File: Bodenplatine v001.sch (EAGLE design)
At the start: 113 parts, among them K1 RY612012, K2 RY612012, K3 RY612012, K4 RY612012, K5 RY612012, K6 RY612012, K7 RY612012, K8 RY612012, K9 RY612012, Q1 BC846BLT1SMD, Q2 BC846BLT1SMD, Q3 BC846BLT1SMD, Q4 BC846BLT1SMD, Q5 BC846BLT1SMD, Q6 BC846BLT1SMD, Q7 BC846BLT1SMD, Q8 BC846BLT1SMD, Q9 BC846BLT1SMD, X1 SPRINGCON_AST125_5X2, X10 SPRINGCON_AST125_3X2, X11 SPRINGCON_AST125_4X2, X12 SPRINGCON_AST125_4X2, X13 SPRINGCON_AST125_5X2, X14 236-403, X15 236-402, X2 SPRINGCON_AST125_5X2, X3 SPRINGCON_AST125_5X2, X4 SPRINGCON_AST125_5X2, X5 SPRINGCON_AST125_5X2, X6 SPRINGCON_AST125_5X2, X7 SPRINGCON_AST125_5X2, X8 SPRINGCON_AST125_5X2, X9 SPRINGCON_AST125_5X2

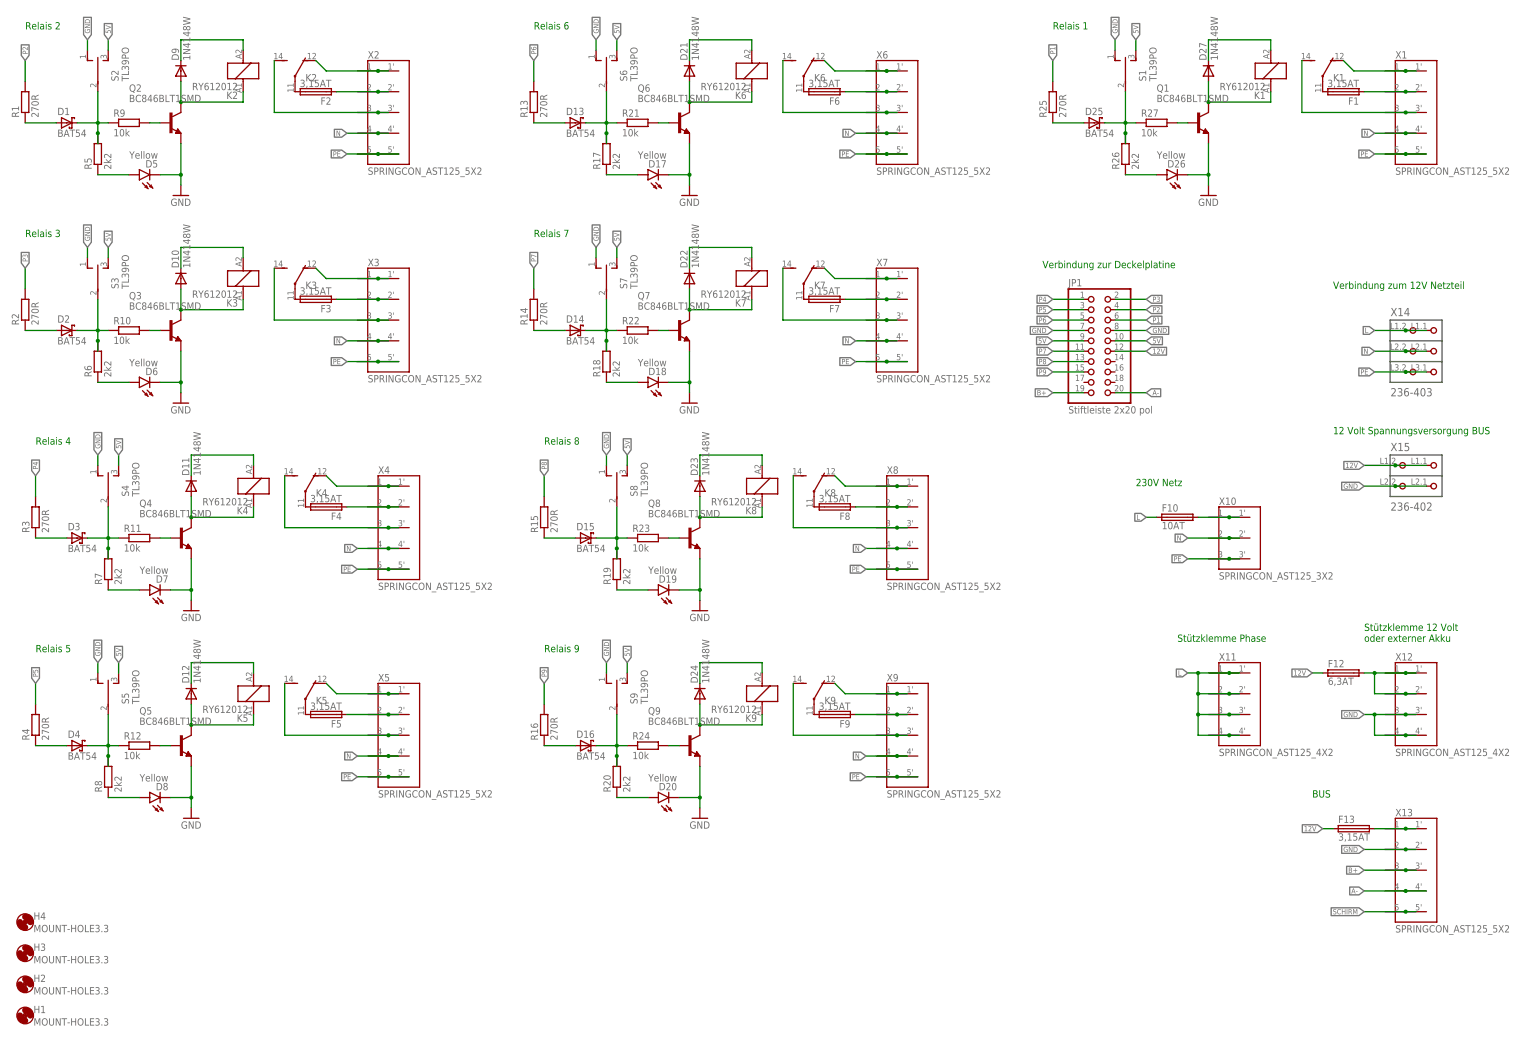
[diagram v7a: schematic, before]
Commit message: Alle Connectoren mit 2 Pins richtig verbunden.@
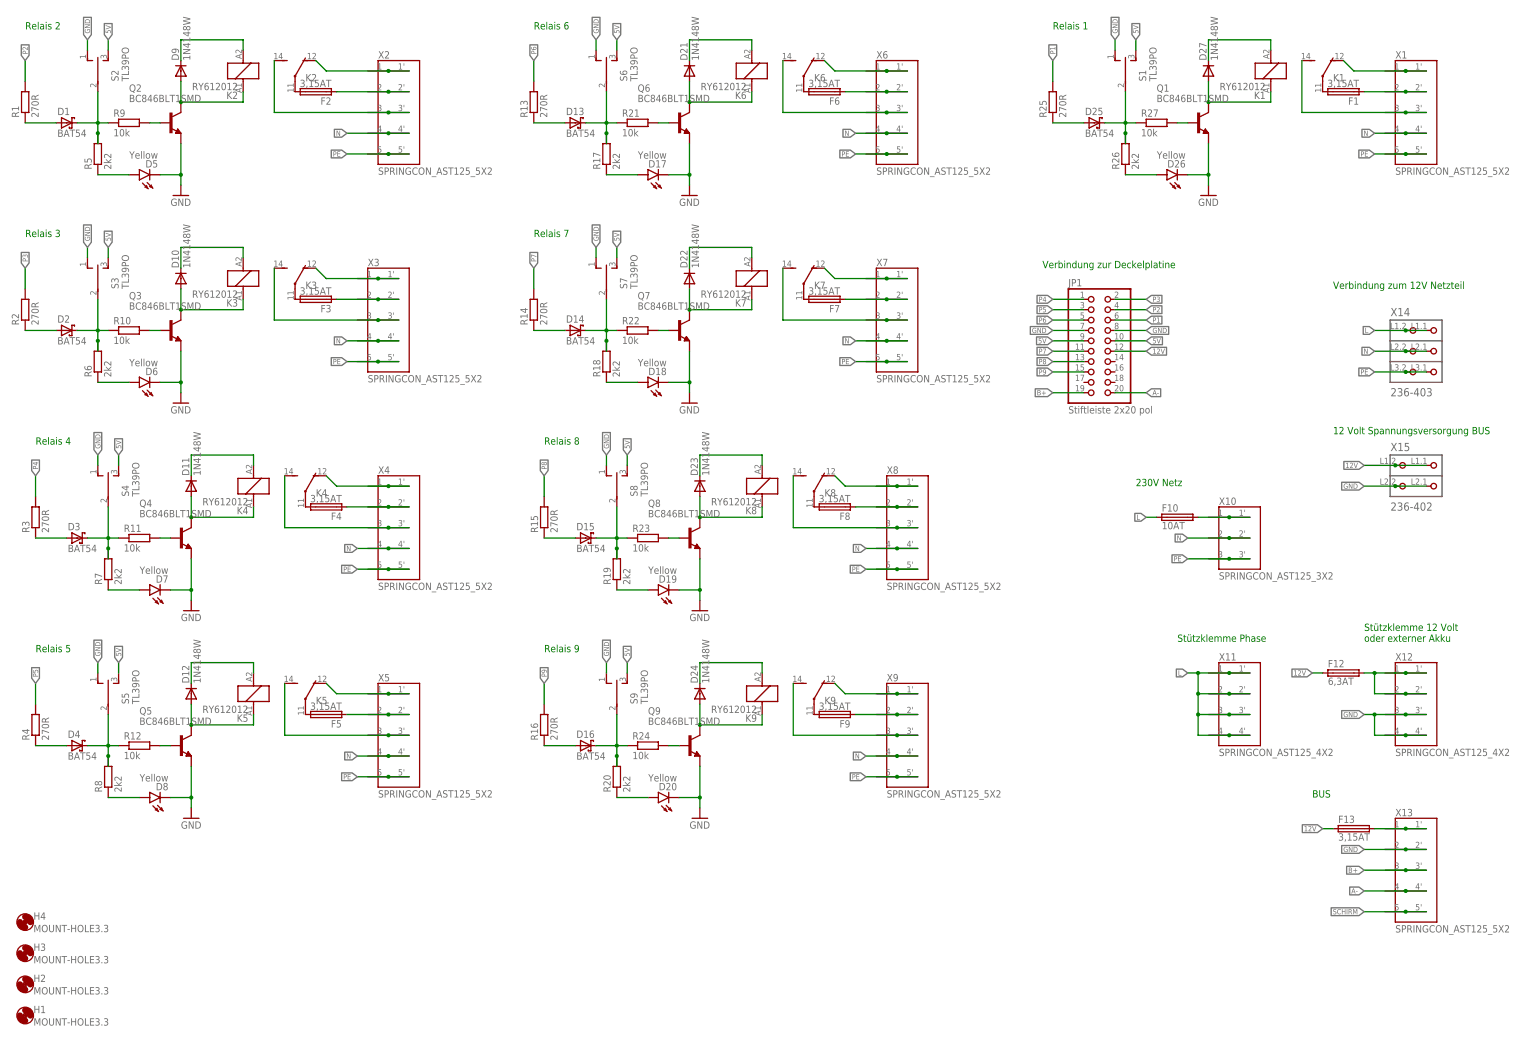
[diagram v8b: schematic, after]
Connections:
- net B+: now also X13.3@2
- net GND: now also X12.3@2, X12.4@2, X13.2@2
- net L: now also X11.1@2, X11.2@2, X11.3@2, X11.4@2
- net N: now also X1.4@2, X10.2@2, X2.4@2, X3.4@2, X4.4@2, X5.4@2, X6.4@2, X7.4@2, X8.4@2, X9.4@2
- net N$1: now also X2.2@2
- net N$19: now also X3.2@2
- net N$2: now also X2.3@2
- net N$20: now also X3.1@2
- net N$21: now also X4.3@2
- net N$29: now also X4.2@2
- net N$30: now also X4.1@2
- net N$31: now also X5.3@2
- net N$39: now also X5.2@2
- net N$4: now also X2.1@2
- net N$40: now also X5.1@2
- net N$41: now also X6.3@2
- net N$49: now also X6.2@2
- net N$50: now also X6.1@2
- net N$51: now also X7.3@2
- net N$59: now also X7.2@2
- net N$6: now also X3.3@2
- net N$60: now also X7.1@2
- net N$61: now also X8.3@2
- net N$69: now also X8.2@2
- net N$70: now also X8.1@2
- net N$71: now also X9.3@2
- net N$79: now also X9.2@2
- net N$80: now also X9.1@2
- net N$81: now also X1.3@2
- net N$89: now also X1.2@2
- net N$90: now also X1.1@2
- net N$91: now also X10.1@2
- net N$92: now also X13.1@2
- net N$94: now also X12.1@2, X12.2@2
- net PE: now also X10.3@2
- net SCHIRM: now also X13.5@2
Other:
- moved on the sheet: X2
